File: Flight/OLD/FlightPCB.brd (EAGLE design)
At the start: 80 x 100 mm, 31 parts

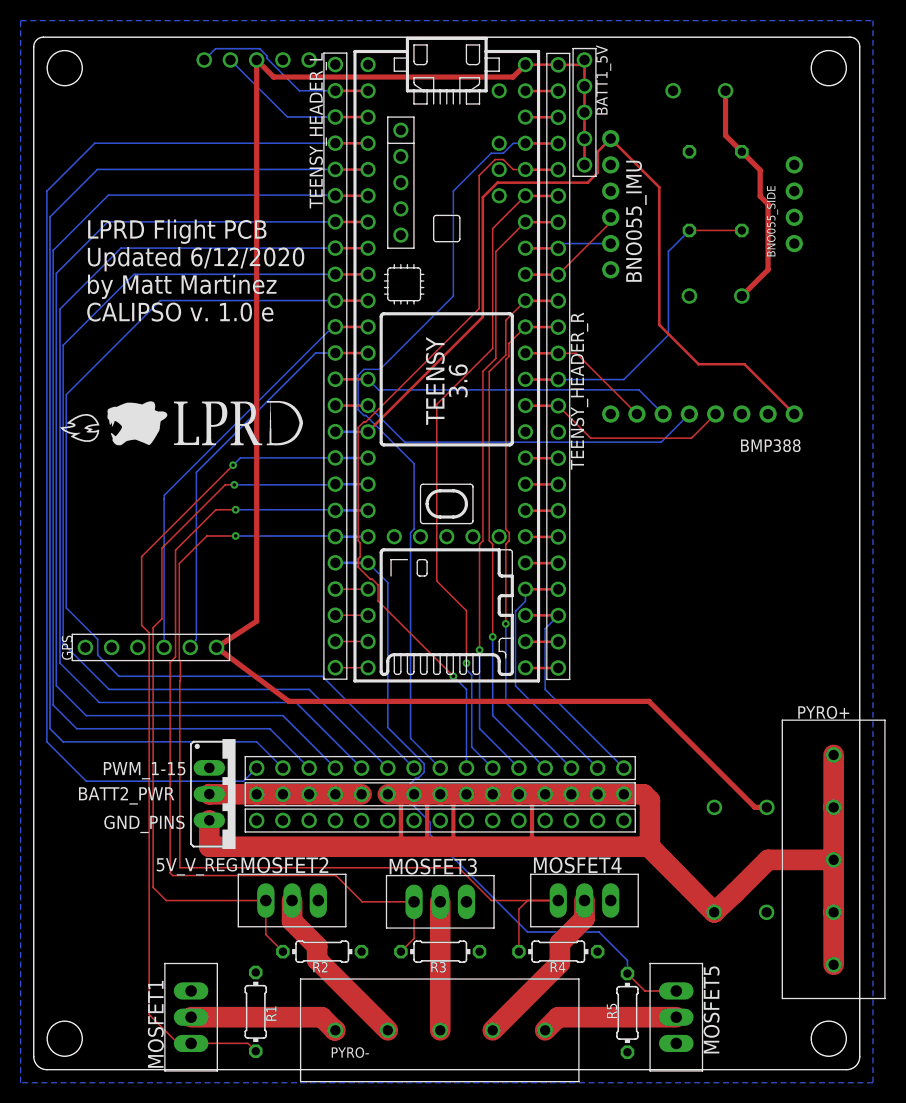
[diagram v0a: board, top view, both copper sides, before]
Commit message: Fixes to Flight PCB
Fixed hole sizing/placement, BEC clearance, GPS clearance, terminal block clearance, resistor hole spacing. Minor silkscreen adjustments
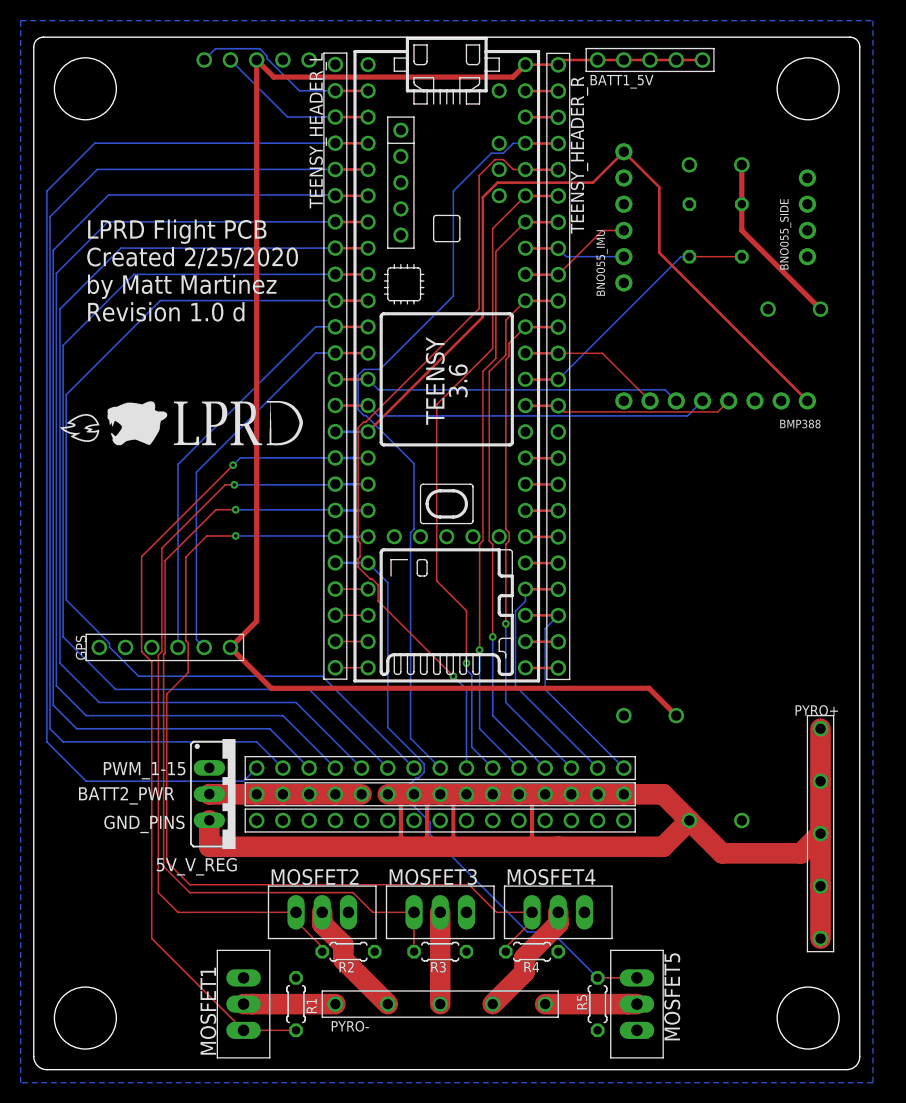
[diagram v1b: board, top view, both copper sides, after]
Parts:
- R1, R2, R3, R4, R5, R6, R7: device rcl:0204/7 -> rcl:0204/5
- moved BEC_OUT 12.5 mm to (62.2, 34.3)
- moved BATT2 9.21 mm to (63.5, 24.1)
- moved BEC_IN 7.73 mm to (76.2, 73.7)
- moved BATT1 7.35 mm to (68.6, 87.6)
- moved MOSFET1 5.24 mm to (14.0, 6.35)
- moved MOSFET5 4.02 mm to (64.8, 6.35)
- moved R1 3.97 mm to (25.4, 6.35)
- moved R6 3.81 mm to (68.6, 81.3)
- moved R7 3.81 mm to (63.5, 81.3)
- moved MOSFET2 3.14 mm to (27.9, 21.6)
- moved R5 3.01 mm to (54.6, 6.35)
- moved BATT1_5V 2.84 mm to (55.9, 97.8), turned to 90 degrees
- moved PYRO+ 2.84 mm to (76.2, 33.0)
- moved MOSFET4 2.79 mm to (50.8, 21.6)
- moved PYRO- 2.54 mm to (29.2, 6.35)
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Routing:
- net +5V: track 161.6 -> 148.4 mm
- net VCC: track 147.4 -> 135.8 mm
- net BATT1_READ_V: track 31.7 -> 25.9 mm
- net CH1: track 14.5 -> 8.89 mm
- net +3V3: track 83.1 -> 77.5 mm
- net BATT1_VCC: track 22.6 -> 17.1 mm
- net PYRO5: track 64.7 -> 59.7 mm
- net CH2: track 16.4 -> 11.5 mm
- net CH4: track 16.3 -> 11.5 mm
- net CH5: track 13.2 -> 8.89 mm
- net PYRO4: track 95.2 -> 91.3 mm
- net CH3: track 12.4 -> 8.89 mm
- net PYRO2: track 72.8 -> 75.0 mm
- net PYRO1: track 82.4 -> 80.9 mm
- net BNO055_SCL: track 8.46 -> 9.87 mm
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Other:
- board text added: "LPRD Flight PCB Created 2/25/2020 by Matt Martinez Revision 1.0 d"
- board text removed: "LPRD Flight PCB Updated 6/12/2020 by Matt Martinez CALIPSO v. 1.0 e"
